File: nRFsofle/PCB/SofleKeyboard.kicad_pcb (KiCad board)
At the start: 2 copper layers, 143.9 x 113.6 mm, 112 parts, among them J1 LED, J2 4PIN, J3 OLED, J4 key leds, J5 backlight sel, J6 indicator bypass, J7 JST_Micro_2, J8 OLED, P1 i2c_pin, P2 i2c_pin, SW1 SW_PUSH-MX_W_LED, SW10 SW_PUSH-MX_W_LED, SW11 SW_PUSH-MX_W_LED, SW12 SW_PUSH-MX_W_LED, SW13 SW_PUSH-MX_W_LED, SW14 SW_PUSH-MX_W_LED, SW15 SW_PUSH-MX_W_LED, SW16 SW_PUSH-MX_W_LED, SW17 SW_PUSH-MX_W_LED, SW18 SW_PUSH-MX_W_LED, SW19 SW_PUSH-MX_W_LED, SW2 SW_PUSH-MX_W_LED, SW20 SW_PUSH-MX_W_LED, SW21 SW_PUSH-MX_W_LED, SW22 SW_PUSH-MX_W_LED, SW23 SW_PUSH-MX_W_LED, SW24 SW_PUSH-MX_W_LED, SW25 Rotary_Encoder_Switch, SW26 SW_PUSH-MX_W_LED, SW27 SW_PUSH-MX_W_LED, SW28 SW_PUSH-MX_W_LED, SW29 SW_PUSH-MX_W_LED, SW3 SW_PUSH-MX_W_LED, SW30 SW_PUSH-MX_W_LED, SW31 SPDT_Switch, SW4 SW_PUSH-MX_W_LED, SW5 SW_PUSH-MX_W_LED, SW6 SW_PUSH-MX_W_LED, SW7 SW_PUSH-MX_W_LED, SW8 SW_PUSH-MX_W_LED, SW9 SW_PUSH-MX_W_LED, U1 nRFMicro

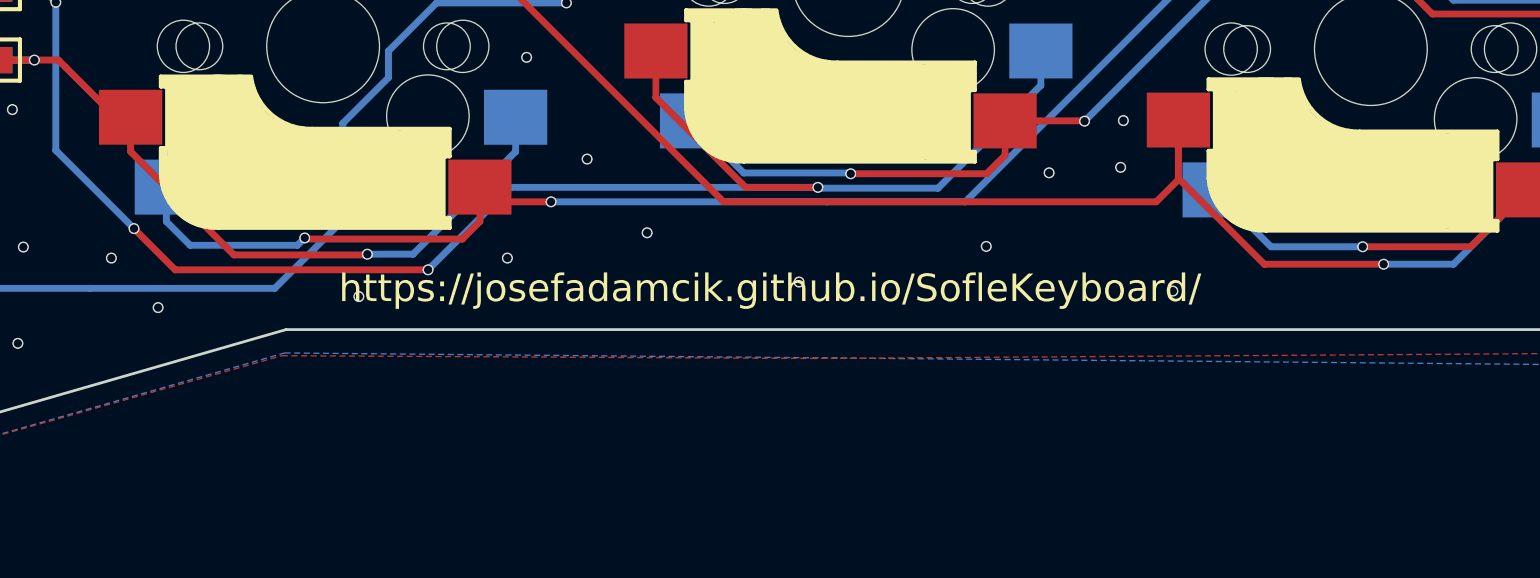
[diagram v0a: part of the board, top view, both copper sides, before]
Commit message: Updated repo url
Now the repository URL printed in the silk layer is updated
to this one.
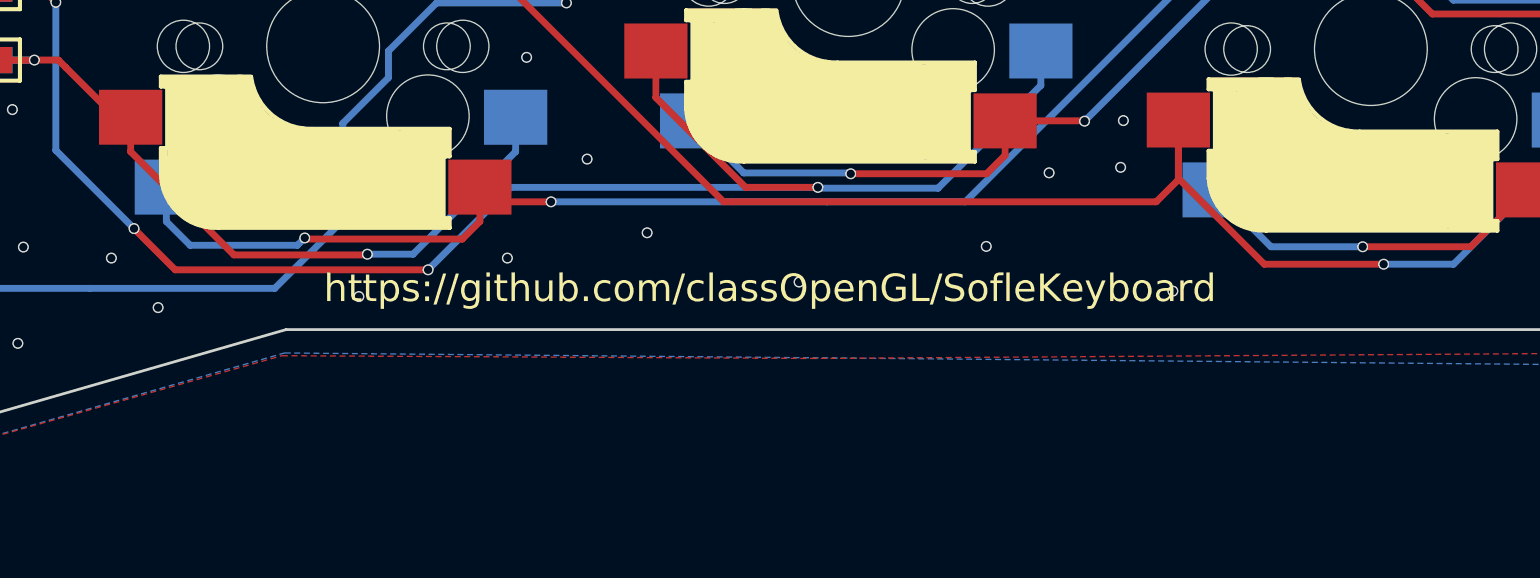
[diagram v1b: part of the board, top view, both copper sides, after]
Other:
- board text added: "https://github.com/classOpenGL/SofleKeyboard"
- board text removed: "https://josefadamcik.github.io/SofleKeyboard/"
